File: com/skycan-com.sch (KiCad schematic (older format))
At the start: 70 parts, among them J1 DF9_25P_1V_PLUG, J2 DF9_25P_1V_SOCKET, J3 DF9_25P_1V_PLUG, J4 DF9_25P_1V_SOCKET, U1 TPS79930, U2 NRF8001, U3 CC112X, U4 UFL, X1 32.768 kHz, X2 16 MHz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

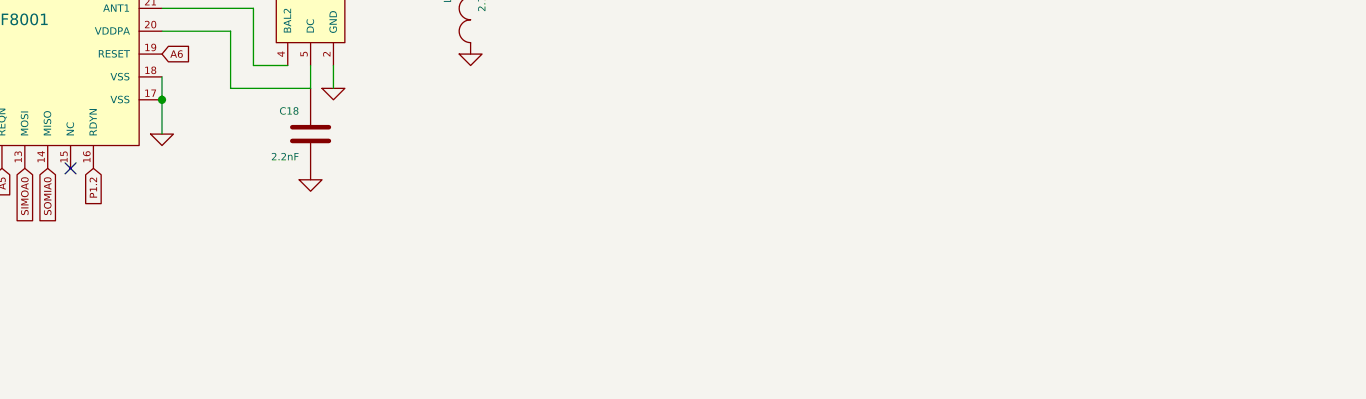
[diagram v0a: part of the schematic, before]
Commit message: add note about BAL1 BAL2 trace lengths
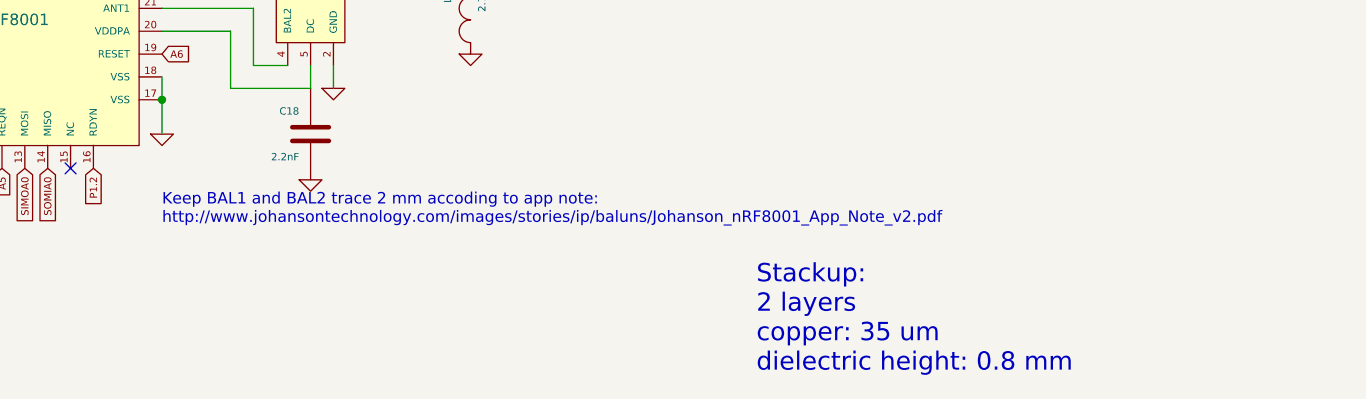
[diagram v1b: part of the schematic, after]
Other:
- note added: "Keep BAL1 and BAL2 trace 2 mm accoding to app note:\nhttp://www.johansontechnology.com/images/stories/ip/baluns/Johanson_nRF8001_App_Note_v2.pdf"
- note added: "Stackup:\n2 layers\ncopper: 35 um\ndielectric height: 0.8 mm \n"
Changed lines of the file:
@@
 F 1 "2450AT18B100" H 11500 7350 60  0000 C CNN
 F 2 "" H 11100 7300 60  0000 C CNN
-F 3 "" H 11100 7300 60  0000 C CNN
+F 3 "http://www.johansontechnology.com/datasheets/antennas/antenna_2450at18b100.pdf" H 11100 7300 60  0001 C CNN
 F 4 "1885497" H 11100 7650 60  0001 C CNN "Farnell"
 	1    11100 7300
@@
 	8100 7250 8100 7150
 Connection ~ 8100 7150
+Text Notes 11800 9450 0    80   ~ 0
+Stackup:\n2 layers\ncopper: 35 um\ndielectric height: 0.8 mm \n
+Text Notes 9200 8800 0    50   ~ 0
+Keep BAL1 and BAL2 trace 2 mm accoding to app note:\nhttp://www.johansontechnology.com/images/stories/ip/baluns/Johanson_nRF8001_App_Note_v2.pdf
 $EndSCHEMATC

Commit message: add part numbers, generate bom
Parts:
- U2: Mouser (none) -> 949-NRF8001-R2Q32-T
- U4: Farnell (none) -> 1688077
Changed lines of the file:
@@
 Sheet 1 1
 Title "COM"
-Date "30 jaan  2014"
+Date "04 märts 2014"
 Rev "1.0"
 Comp "Skycan"
@@
 F 2 "" H 14950 3850 60  0000 C CNN
 F 3 "" H 14950 3850 60  0000 C CNN
+F 4 "1688077" H 14950 3850 60  0001 C CNN "Farnell"
 	1    14950 3850
 	1    0    0    -1
@@
 F 2 "" H 8550 7900 60  0000 C CNN
 F 3 "" H 8550 7900 60  0000 C CNN
+F 4 "949-NRF8001-R2Q32-T" H 8550 7900 60  0001 C CNN "Mouser"
 	1    8550 7900
 	1    0    0    -1
